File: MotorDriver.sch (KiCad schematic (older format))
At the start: 0 parts

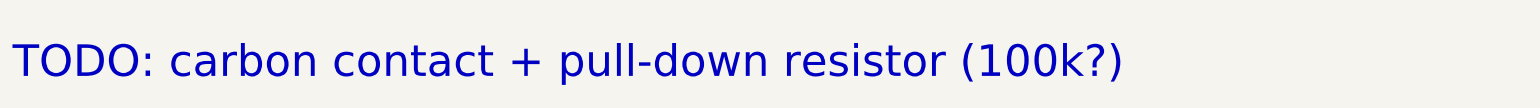
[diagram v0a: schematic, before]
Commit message: Add placeholder sheets for functions to be implemented
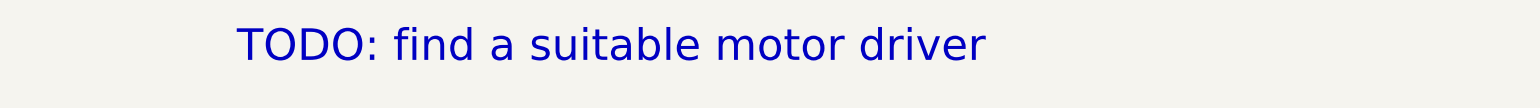
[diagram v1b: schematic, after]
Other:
- note added: "TODO: find a suitable motor driver"
- note removed: "TODO: carbon contact + pull-down resistor (100k?)"
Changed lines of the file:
@@
 $Descr A4 11693 8268
 encoding utf-8
-Sheet 10 16
-Title "Litter Robot 3 - Push button"
-Date "2021-02-28"
+Sheet 16 16
+Title "Litter Robot 3 - Motor driver"
+Date "2021-03-02"
 Rev "A1"
 Comp "L. Sartory"
@@
 Comment4 ""
 $EndDescr
-Text Notes 2000 4100 0    197  ~ 0
-TODO: carbon contact + pull-down resistor (100k?)
+Text Notes 3400 4000 0    197  ~ 0
+TODO: find a suitable motor driver
 $EndSCHEMATC

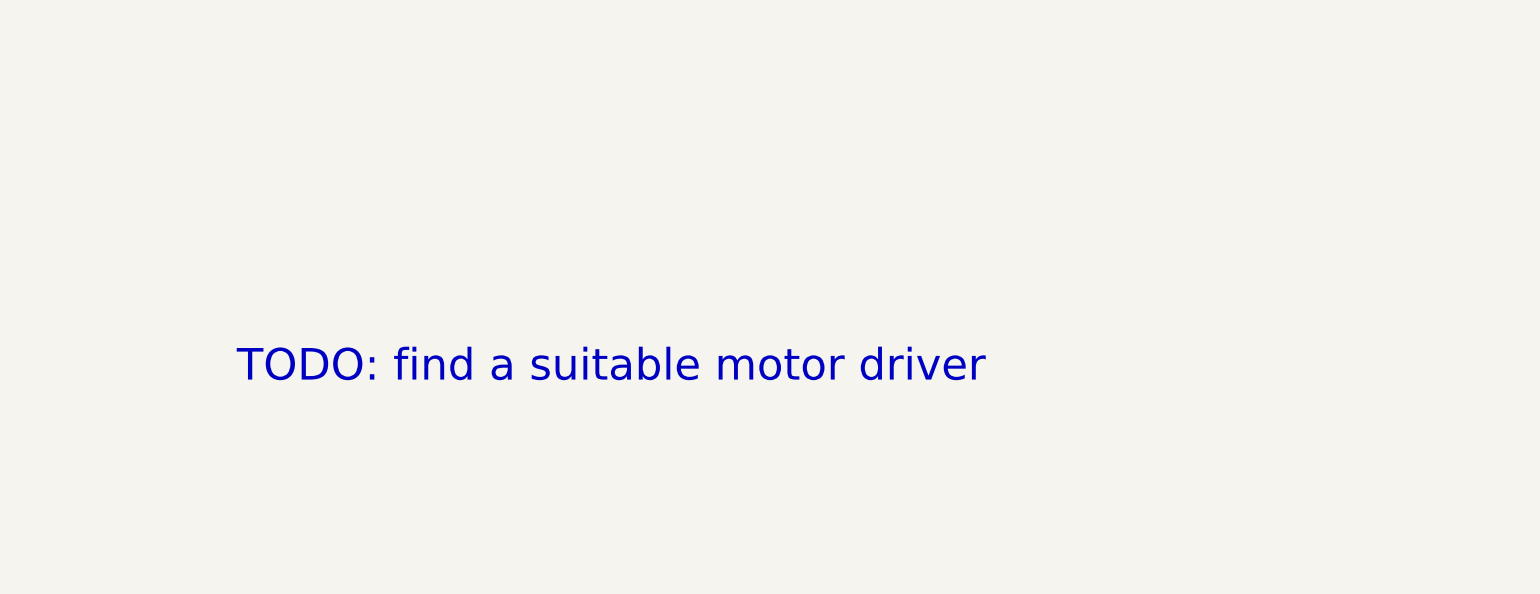
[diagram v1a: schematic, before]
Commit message: Add the power supply and motor driver ICs
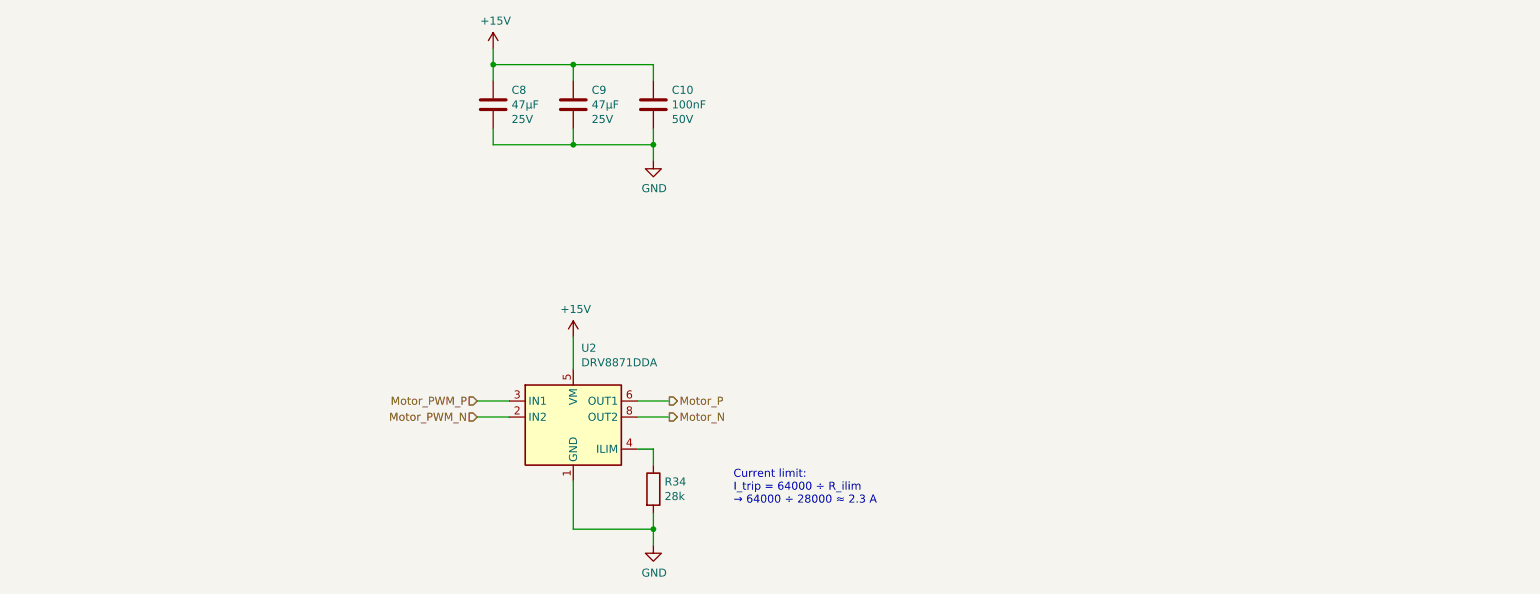
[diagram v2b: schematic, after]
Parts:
- added C10: 100nF, Capacitor_SMD:C_0603_1608Metric, symbol Device:C
- added C8, C9: 47µF, Capacitor_SMD:C_0603_1608Metric, symbol Device:C
- added R34: 28k, Resistor_SMD:R_0603_1608Metric, symbol Device:R
- added U2: DRV8871DDA, Package_SO:Texas_HTSOP-8-1EP_3.9x4.9mm_P1.27mm_EP2.95x4.9mm_Mask2.4x3.1mm_ThermalVias, symbol Driver_Motor:DRV8871DDA
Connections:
- new net: R34.1, U2.4 (ILIM)
- new net +15V: C10.1, C8.1, C9.1, U2.5 (VM)
- new net GND: C10.2, C8.2, C9.2, R34.2, U2.1 (GND), U2.7 (GND), U2.9 (GND)
- new net Motor_N: U2.8 (OUT2)
- new net Motor_P: U2.6 (OUT1)
- new net Motor_PWM_N: U2.2 (IN2)
- new net Motor_PWM_P: U2.3 (IN1)
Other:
- note added: "Current limit:\nI_trip = 64000 ÷ R_ilim\n→ 64000 ÷ 28000 ≈ 2.3 A"
- note removed: "TODO: find a suitable motor driver"
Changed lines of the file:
@@
 Comment4 ""
 $EndDescr
-Text Notes 3400 4000 0    197  ~ 0
-TODO: find a suitable motor driver
+$Comp
+L Device:C C10
+U 1 1 6044E535
+P 6000 2250
+F 0 "C10" H 6115 2341 50  0000 L CNN
+F 1 "100nF" H 6115 2250 50  0000 L CNN
+F 2 "Capacitor_SMD:C_0603_1608Metric" H 6038 2100 50  0001 C CNN
+F 3 "~" H 6000 2250 50  0001 C CNN
+F 4 "C1608X5R1H104K080AA" H 6000 2250 50  0001 C CNN "Part_Number"
+F 5 "50V" H 6115 2159 50  0000 L CNN "Voltage"
+	1    6000 2250
+	1    0    0    -1
+$EndComp
+$Comp
+L Device:C C8
+U 1 1 60452EC0
+P 5000 2250
+F 0 "C8" H 5115 2341 50  0000 L CNN
+F 1 "47µF" H 5115 2250 50  0000 L CNN
+F 2 "Capacitor_SMD:C_0603_1608Metric" H 5038 2100 50  0001 C CNN
+F 3 "~" H 5000 2250 50  0001 C CNN
+F 4 "C3216X5R1E476M160AC" H 5000 2250 50  0001 C CNN "Part_Number"
+F 5 "25V" H 5115 2159 50  0000 L CNN "Voltage"
+	1    5000 2250
+	1    0    0    -1
+$EndComp
+$Comp
+L Device:C C9
+U 1 1 6045368C
+P 5500 2250
+F 0 "C9" H 5615 2341 50  0000 L CNN
+F 1 "47µF" H 5615 2250 50  0000 L CNN
+F 2 "Capacitor_SMD:C_0603_1608Metric" H 5538 2100 50  0001 C CNN
+F 3 "~" H 5500 2250 50  0001 C CNN
+F 4 "C3216X5R1E476M160AC" H 5500 2250 50  0001 C CNN "Part_Number"
+F 5 "25V" H 5615 2159 50  0000 L CNN "Voltage"
+	1    5500 2250
+	1    0    0    -1
+$EndComp
+Wire Wire Line
+	5500 3900 5500 3700
+$Comp
+L power:+15V #PWR052
+U 1 1 60454ACA
+P 5500 3700
+F 0 "#PWR052" H 5500 3550 50  0001 C CNN
+F 1 "+15V" H 5515 3873 50  0000 C CNN
+F 2 "" H 5500 3700 50  0001 C CNN
+F 3 "" H 5500 3700 50  0001 C CNN
+	1    5500 3700
+	1    0    0    -1
+$EndComp
+$Comp
+L power:+15V #PWR051
+U 1 1 60457C46
+P 5000 1900
+F 0 "#PWR051" H 5000 1750 50  0001 C CNN
+F 1 "+15V" H 5015 2073 50  0000 C CNN
+F 2 "" H 5000 1900 50  0001 C CNN
+F 3 "" H 5000 1900 50  0001 C CNN
+	1    5000 1900
+	1    0    0    -1
+$EndComp
+$Comp
+L power:GND #PWR053
+U 1 1 604586C2
+P 6000 2600
+F 0 "#PWR053" H 6000 2350 50  0001 C CNN
+F 1 "GND" H 6005 2427 50  0000 C CNN
+F 2 "" H 6000 2600 50  0001 C CNN
+F 3 "" H 6000 2600 50  0001 C CNN
+	1    6000 2600
+	1    0    0    -1
+$EndComp
+Wire Wire Line
+	5000 2400 5000 2500
+Wire Wire Line
+	5000 2500 5500 2500
+Wire Wire Line
+	6000 2500 6000 2600
+Wire Wire Line
+	6000 2100 6000 2000
+Wire Wire Line
+	6000 2000 5500 2000
+Wire Wire Line
+	5000 2000 5000 1900
+Wire Wire Line
+	5000 2100 5000 2000
+Connection ~ 5000 2000
+Wire Wire Line
+	5500 2000 5500 2100
+Wire Wire Line
+	5500 2400 5500 2500
+Connection ~ 5500 2000
+Wire Wire Line
+	5500 2000 5000 2000
+Connection ~ 5500 2500
+Wire Wire Line
+	5500 2500 6000 2500
+Wire Wire Line
+	6000 2400 6000 2500
+Connection ~ 6000 2500
+Text HLabel 4900 4100 0    50   Input ~ 0
+Motor_PWM_P
+Text HLabel 4900 4200 0    50   Input ~ 0
+Motor_PWM_N
+Wire Wire Line
+	4900 4100 5100 4100
+Wire Wire Line
+	5100 4200 4900 4200
+Text HLabel 6100 4100 2    50   Output ~ 0
+Motor_P
+Text HLabel 6100 4200 2    50   Output ~ 0
+Motor_N
+Wire Wire Line
+	5900 4100 6100 4100
+Wire Wire Line
+	5900 4200 6100 4200
+$Comp
+L power:GND #PWR054
+U 1 1 6046463F
+P 6000 5000
+F 0 "#PWR054" H 6000 4750 50  0001 C CNN
+F 1 "GND" H 6005 4827 50  0000 C CNN
+F 2 "" H 6000 5000 50  0001 C CNN
+F 3 "" H 6000 5000 50  0001 C CNN
+	1    6000 5000
+	1    0    0    -1
+$EndComp
+Wire Wire Line
+	6000 5000 6000 4900
+Wire Wire Line
+	6000 4900 5500 4900
+Wire Wire Line
+	5500 4600 5500 4900
+Connection ~ 6000 4900
+Wire Wire Line
+	6000 4900 6000 4800
+Wire Wire Line
+	5900 4400 6000 4400
+Wire Wire Line
+	6000 4400 6000 4500
+$Comp
+L Device:R R34
+U 1 1 604667F9
+P 6000 4650
+F 0 "R34" H 6070 4696 50  0000 L CNN
+F 1 "28k" H 6070 4605 50  0000 L CNN
+F 2 "Resistor_SMD:R_0603_1608Metric" V 5930 4650 50  0001 C CNN
+F 3 "~" H 6000 4650 50  0001 C CNN
+F 4 "CR0603-FX-2802ELF" H 6000 4650 50  0001 C CNN "Part_Number"
+	1    6000 4650
+	1    0    0    -1
+$EndComp
+Text Notes 6500 4750 0    50   ~ 0
+Current limit:\nI_trip = 64000 ÷ R_ilim\n→ 64000 ÷ 28000 ≈ 2.3 A
+$Comp
+L Driver_Motor:DRV8871DDA U2
+U 1 1 6044D886
+P 5500 4200
+F 0 "U2" H 5550 4631 50  0000 L CNN
+F 1 "DRV8871DDA" H 5550 4540 50  0000 L CNN
+F 2 "Package_SO:Texas_HTSOP-8-1EP_3.9x4.9mm_P1.27mm_EP2.95x4.9mm_Mask2.4x3.1mm_ThermalVias" H 5750 4150 50  0001 C CNN
+F 3 "http://www.ti.com/lit/ds/symlink/drv8871.pdf" H 5750 4150 50  0001 C CNN
+F 4 "DRV8871DDARQ1" H 5500 4200 50  0001 C CNN "Part_Number"
+	1    5500 4200
+	1    0    0    -1
+$EndComp
 $EndSCHEMATC

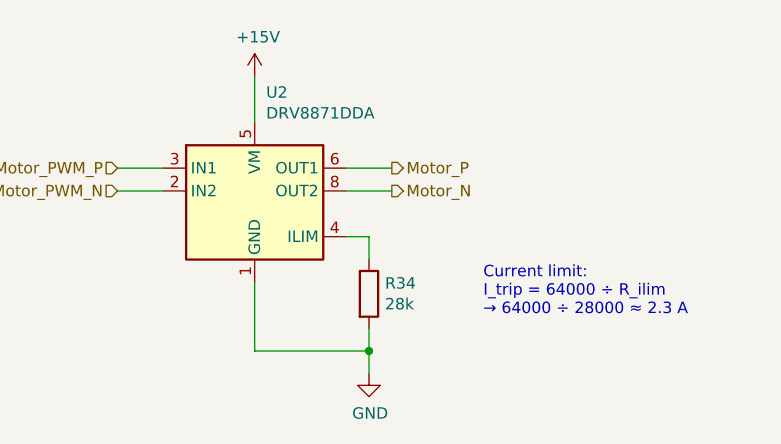
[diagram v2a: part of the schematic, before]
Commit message: Add the push buttons and mounting holes
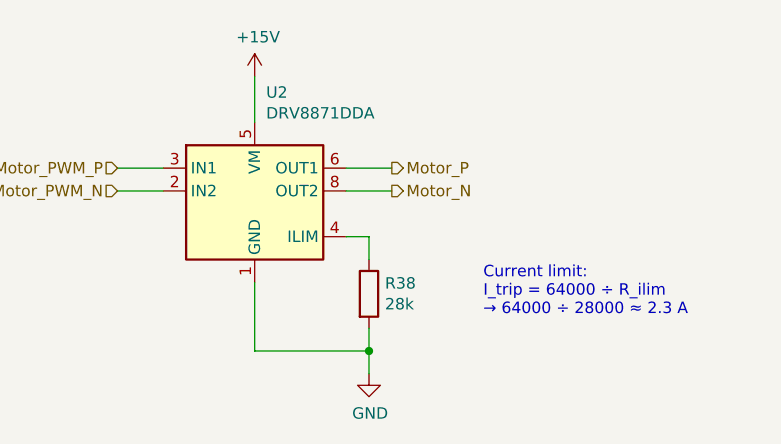
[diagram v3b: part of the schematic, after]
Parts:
- renumbered R34 to R38
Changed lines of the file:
@@
 	5500 3900 5500 3700
 $Comp
-L power:+15V #PWR052
+L power:+15V #PWR060
 U 1 1 60454ACA
 P 5500 3700
-F 0 "#PWR052" H 5500 3550 50  0001 C CNN
+F 0 "#PWR060" H 5500 3550 50  0001 C CNN
 F 1 "+15V" H 5515 3873 50  0000 C CNN
 F 2 "" H 5500 3700 50  0001 C CNN
@@
 $EndComp
 $Comp
-L power:+15V #PWR051
+L power:+15V #PWR059
 U 1 1 60457C46
 P 5000 1900
-F 0 "#PWR051" H 5000 1750 50  0001 C CNN
+F 0 "#PWR059" H 5000 1750 50  0001 C CNN
 F 1 "+15V" H 5015 2073 50  0000 C CNN
 F 2 "" H 5000 1900 50  0001 C CNN
@@
 $EndComp
 $Comp
-L power:GND #PWR053
+L power:GND #PWR061
 U 1 1 604586C2
 P 6000 2600
-F 0 "#PWR053" H 6000 2350 50  0001 C CNN
+F 0 "#PWR061" H 6000 2350 50  0001 C CNN
 F 1 "GND" H 6005 2427 50  0000 C CNN
 F 2 "" H 6000 2600 50  0001 C CNN
@@
 	5900 4200 6100 4200
 $Comp
-L power:GND #PWR054
+L power:GND #PWR062
 U 1 1 6046463F
 P 6000 5000
-F 0 "#PWR054" H 6000 4750 50  0001 C CNN
+F 0 "#PWR062" H 6000 4750 50  0001 C CNN
 F 1 "GND" H 6005 4827 50  0000 C CNN
 F 2 "" H 6000 5000 50  0001 C CNN
@@
 	6000 4400 6000 4500
 $Comp
-L Device:R R34
+L Device:R R38
 U 1 1 604667F9
 P 6000 4650
-F 0 "R34" H 6070 4696 50  0000 L CNN
+F 0 "R38" H 6070 4696 50  0000 L CNN
 F 1 "28k" H 6070 4605 50  0000 L CNN
 F 2 "Resistor_SMD:R_0603_1608Metric" V 5930 4650 50  0001 C CNN

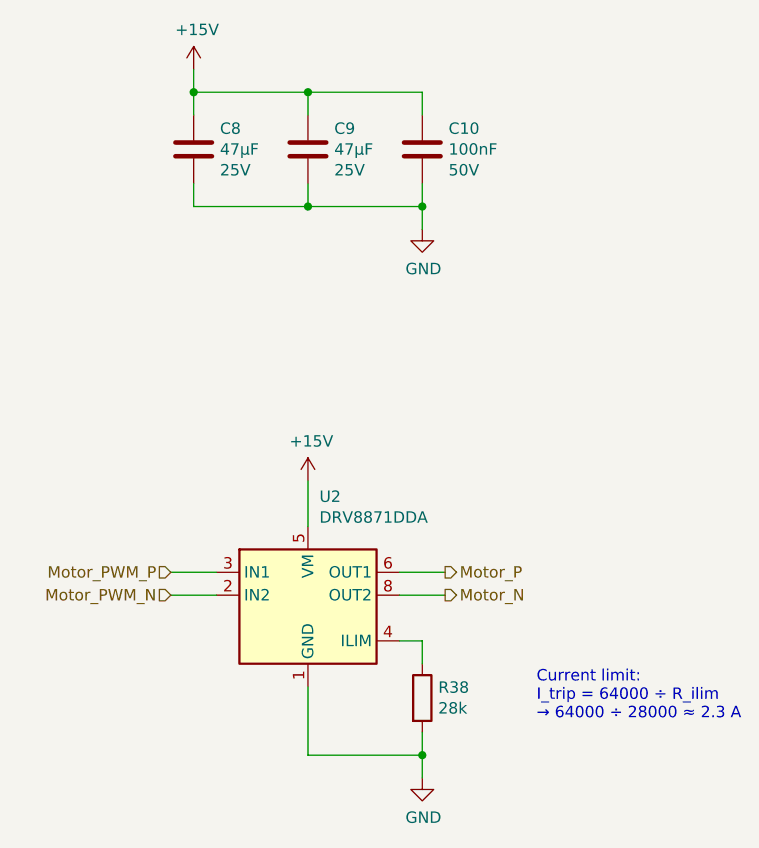
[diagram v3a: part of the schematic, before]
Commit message: Add fuse and more inter-page signals
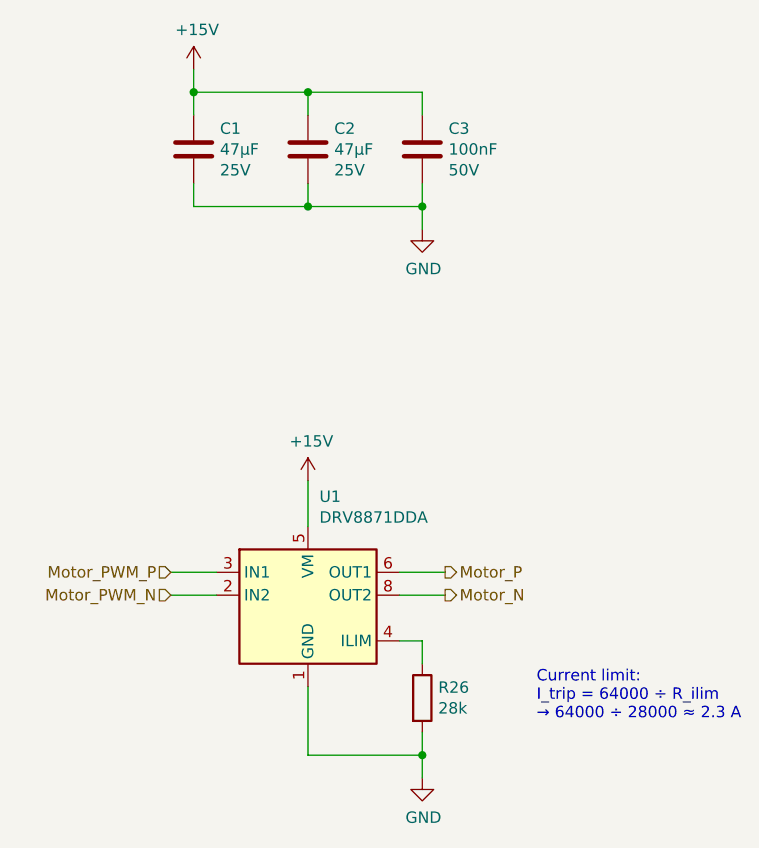
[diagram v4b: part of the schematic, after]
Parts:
- renumbered C8 to C1, C9 to C2, C10 to C3, R38 to R26, U2 to U1
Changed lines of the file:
@@
 $Descr A4 11693 8268
 encoding utf-8
-Sheet 16 16
+Sheet 14 16
 Title "Litter Robot 3 - Motor driver"
 Date "2021-03-02"
@@
 $EndDescr
 $Comp
-L Device:C C10
+L Device:C C3
 U 1 1 6044E535
 P 6000 2250
-F 0 "C10" H 6115 2341 50  0000 L CNN
+F 0 "C3" H 6115 2341 50  0000 L CNN
 F 1 "100nF" H 6115 2250 50  0000 L CNN
 F 2 "Capacitor_SMD:C_0603_1608Metric" H 6038 2100 50  0001 C CNN
@@
 $EndComp
 $Comp
-L Device:C C8
+L Device:C C1
 U 1 1 60452EC0
 P 5000 2250
-F 0 "C8" H 5115 2341 50  0000 L CNN
+F 0 "C1" H 5115 2341 50  0000 L CNN
 F 1 "47µF" H 5115 2250 50  0000 L CNN
 F 2 "Capacitor_SMD:C_0603_1608Metric" H 5038 2100 50  0001 C CNN
@@
 $EndComp
 $Comp
-L Device:C C9
+L Device:C C2
 U 1 1 6045368C
 P 5500 2250
-F 0 "C9" H 5615 2341 50  0000 L CNN
+F 0 "C2" H 5615 2341 50  0000 L CNN
 F 1 "47µF" H 5615 2250 50  0000 L CNN
 F 2 "Capacitor_SMD:C_0603_1608Metric" H 5538 2100 50  0001 C CNN
@@
 	5500 3900 5500 3700
 $Comp
-L power:+15V #PWR060
+L power:+15V #PWR049
 U 1 1 60454ACA
 P 5500 3700
-F 0 "#PWR060" H 5500 3550 50  0001 C CNN
+F 0 "#PWR049" H 5500 3550 50  0001 C CNN
 F 1 "+15V" H 5515 3873 50  0000 C CNN
 F 2 "" H 5500 3700 50  0001 C CNN
@@
 $EndComp
 $Comp
-L power:+15V #PWR059
+L power:+15V #PWR048
 U 1 1 60457C46
 P 5000 1900
-F 0 "#PWR059" H 5000 1750 50  0001 C CNN
+F 0 "#PWR048" H 5000 1750 50  0001 C CNN
 F 1 "+15V" H 5015 2073 50  0000 C CNN
 F 2 "" H 5000 1900 50  0001 C CNN
@@
 $EndComp
 $Comp
-L power:GND #PWR061
+L power:GND #PWR050
 U 1 1 604586C2
 P 6000 2600
-F 0 "#PWR061" H 6000 2350 50  0001 C CNN
+F 0 "#PWR050" H 6000 2350 50  0001 C CNN
 F 1 "GND" H 6005 2427 50  0000 C CNN
 F 2 "" H 6000 2600 50  0001 C CNN
@@
 	5900 4200 6100 4200
 $Comp
-L power:GND #PWR062
+L power:GND #PWR051
 U 1 1 6046463F
 P 6000 5000
-F 0 "#PWR062" H 6000 4750 50  0001 C CNN
+F 0 "#PWR051" H 6000 4750 50  0001 C CNN
 F 1 "GND" H 6005 4827 50  0000 C CNN
 F 2 "" H 6000 5000 50  0001 C CNN
@@
 	6000 4400 6000 4500
 $Comp
-L Device:R R38
+L Device:R R26
 U 1 1 604667F9
 P 6000 4650
-F 0 "R38" H 6070 4696 50  0000 L CNN
+F 0 "R26" H 6070 4696 50  0000 L CNN
 F 1 "28k" H 6070 4605 50  0000 L CNN
 F 2 "Resistor_SMD:R_0603_1608Metric" V 5930 4650 50  0001 C CNN
@@
 Current limit:\nI_trip = 64000 ÷ R_ilim\n→ 64000 ÷ 28000 ≈ 2.3 A
 $Comp
-L Driver_Motor:DRV8871DDA U2
+L Driver_Motor:DRV8871DDA U1
 U 1 1 6044D886
 P 5500 4200
-F 0 "U2" H 5550 4631 50  0000 L CNN
+F 0 "U1" H 5550 4631 50  0000 L CNN
 F 1 "DRV8871DDA" H 5550 4540 50  0000 L CNN
 F 2 "Package_SO:Texas_HTSOP-8-1EP_3.9x4.9mm_P1.27mm_EP2.95x4.9mm_Mask2.4x3.1mm_ThermalVias" H 5750 4150 50  0001 C CNN
